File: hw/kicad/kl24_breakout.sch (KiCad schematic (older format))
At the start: 69 parts, among them J1 USB-micro-ab, J2 ARM_10PIN, P1 BATT+, P10 TST, P11 TST, P12 TST, P13 TST, P14 TST, P15 TST, P16 TST, P17 TST, P18 TST, P19 TST, P2 BATT-, P20 TST, P21 TST, P22 TST, P23 TST, P24 TST, P25 TST, P26 TST, P27 TST, P28 TST, P29 TST, P3 BATT_BACKUP+, P30 TST, P31 TST, P32 TST, P33 TST, P34 TST, P35 TST, P36 TST, P4 BATT_BACKUP-, P5 TST, P6 TST, P7 TST, P8 TST, P9 TST, U1 MCP1252-33X50I, U2 MCP73831, U3 MKL24Z64VFM4, U4 MCP1640_SOT23, U5 LP3985, U6 M25P05-A, X1 CRYSTAL

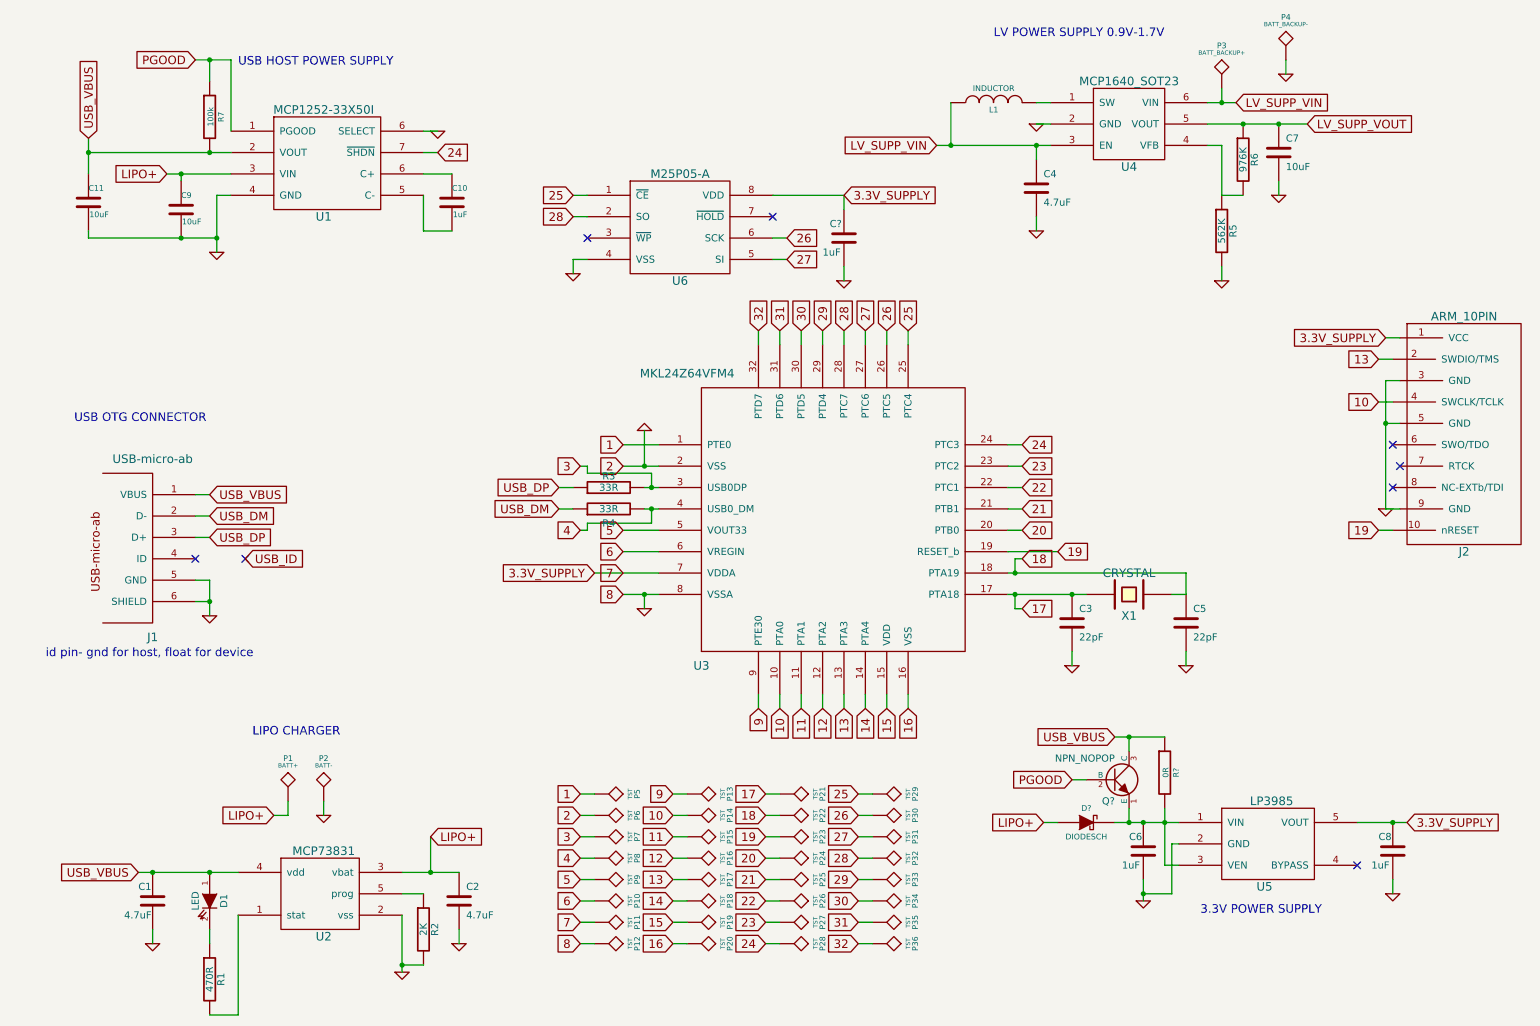
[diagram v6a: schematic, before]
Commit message: - remove usb host pwr supply, sch done.
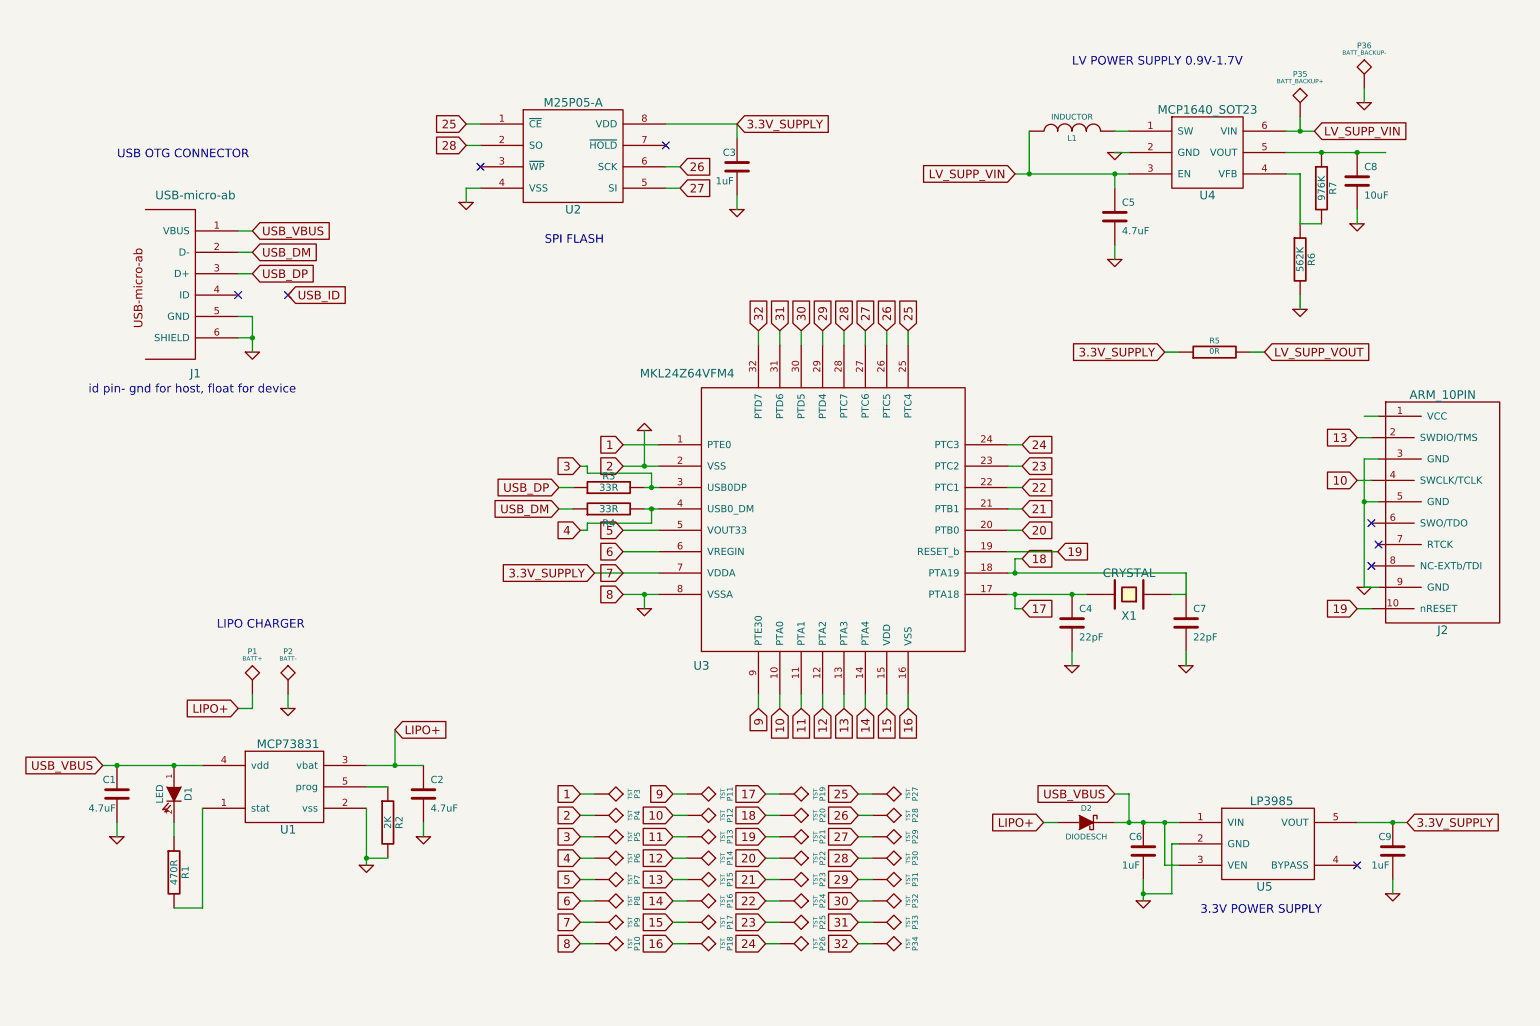
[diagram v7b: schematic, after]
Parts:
- removed C10: 1uF, ~, symbol C
- removed C11, C9: 10uF, ~, symbol C
- removed Q?: NPN_NOPOP, ~, symbol NPN
- removed R7: 100k, ~, symbol R
- removed R?: 0R, ~, symbol R
- removed U1: MCP1252-33X50I, symbol MCP1252-33X50I
- added R5: 0R, ~, symbol R
- gave numbers to parts that had none: 2
- renumbered C3 to C4, C4 to C5, C5 to C7, C7 to C8, C8 to C9, P12 to P10, P13 to P11, P14 to P12, P15 to P13, P16 to P14, P17 to P15, P18 to P16, P19 to P17, P20 to P18, P21 to P19, P22 to P20, P23 to P21, P24 to P22, P25 to P23, P26 to P24, P27 to P25, P28 to P26, P29 to P27, P30 to P28, P31 to P29, P5 to P3, P32 to P30, P33 to P31, P34 to P32, P35 to P33, P36 to P34, P3 to P35, P4 to P36, P6 to P4, P7 to P5, P8 to P6, P9 to P7, P10 to P8, P11 to P9, R5 to R6, R6 to R7, U2 to U1, U6 to U2
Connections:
- net 3.3V_SUPPLY: now also R5.1; no longer J2.1 (VCC)
- net LV_SUPP_VOUT: now also R5.2; no longer C8.1, R7.1, U4.5 (VOUT)
- net USB_VBUS: now also C6.1, D2.2 (K), U5.1 (VIN), U5.3 (VEN)
- new net: C8.1, R7.1, U4.5 (VOUT)
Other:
- note added: "SPI FLASH"
- note removed: "USB HOST POWER SUPPLY"
- moved on the sheet: C1, C2, C3, C5, C8, D1, J1, J2, L1, P1, P2, P35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
